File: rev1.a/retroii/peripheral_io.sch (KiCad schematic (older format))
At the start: 24 parts, among them J12 Peripheral Slot 0, J15 Peripheral Slot 4, J16 Peripheral Slot 1, J17 Peripheral Slot 5, J18 Peripheral Slot 2, J19 Peripheral Slot 6, J20 Peripheral Slot 3, J21 Peripheral Slot 7

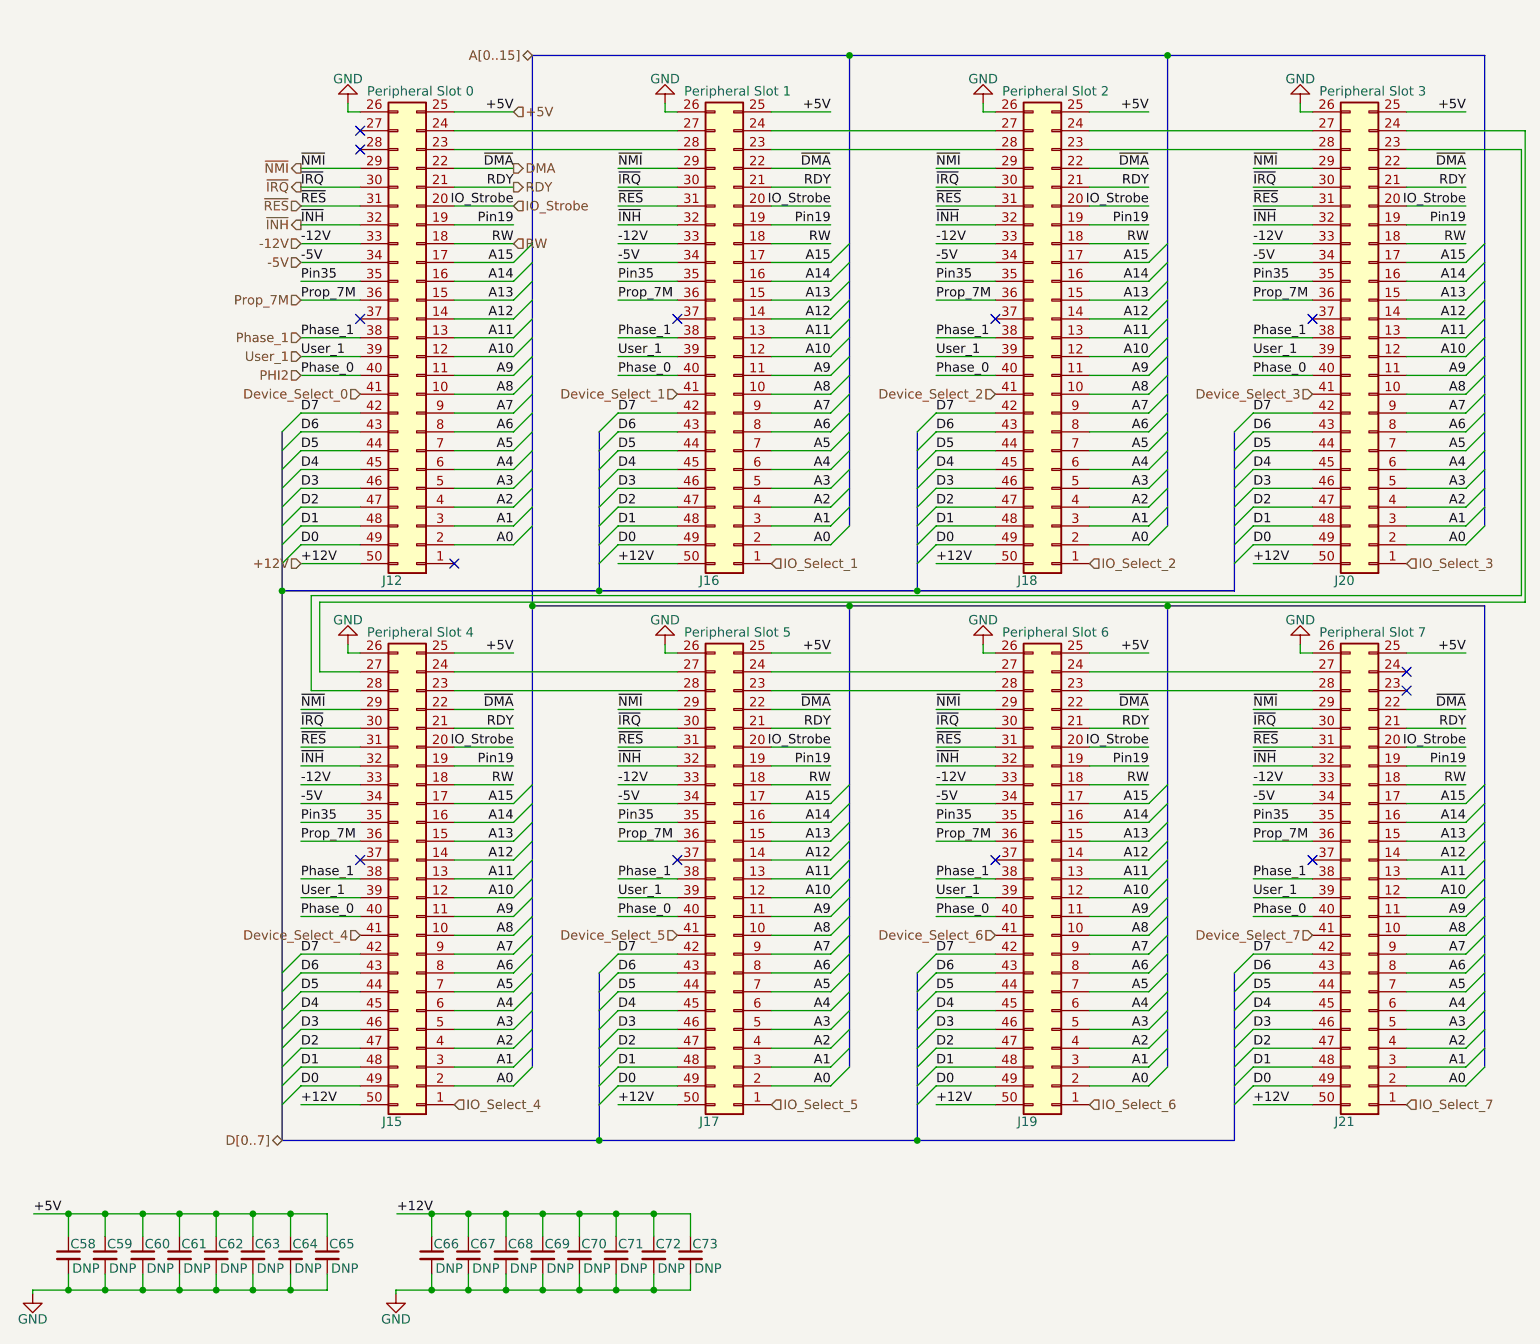
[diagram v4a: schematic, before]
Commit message: added prop_q3 to peripheral slot connections.
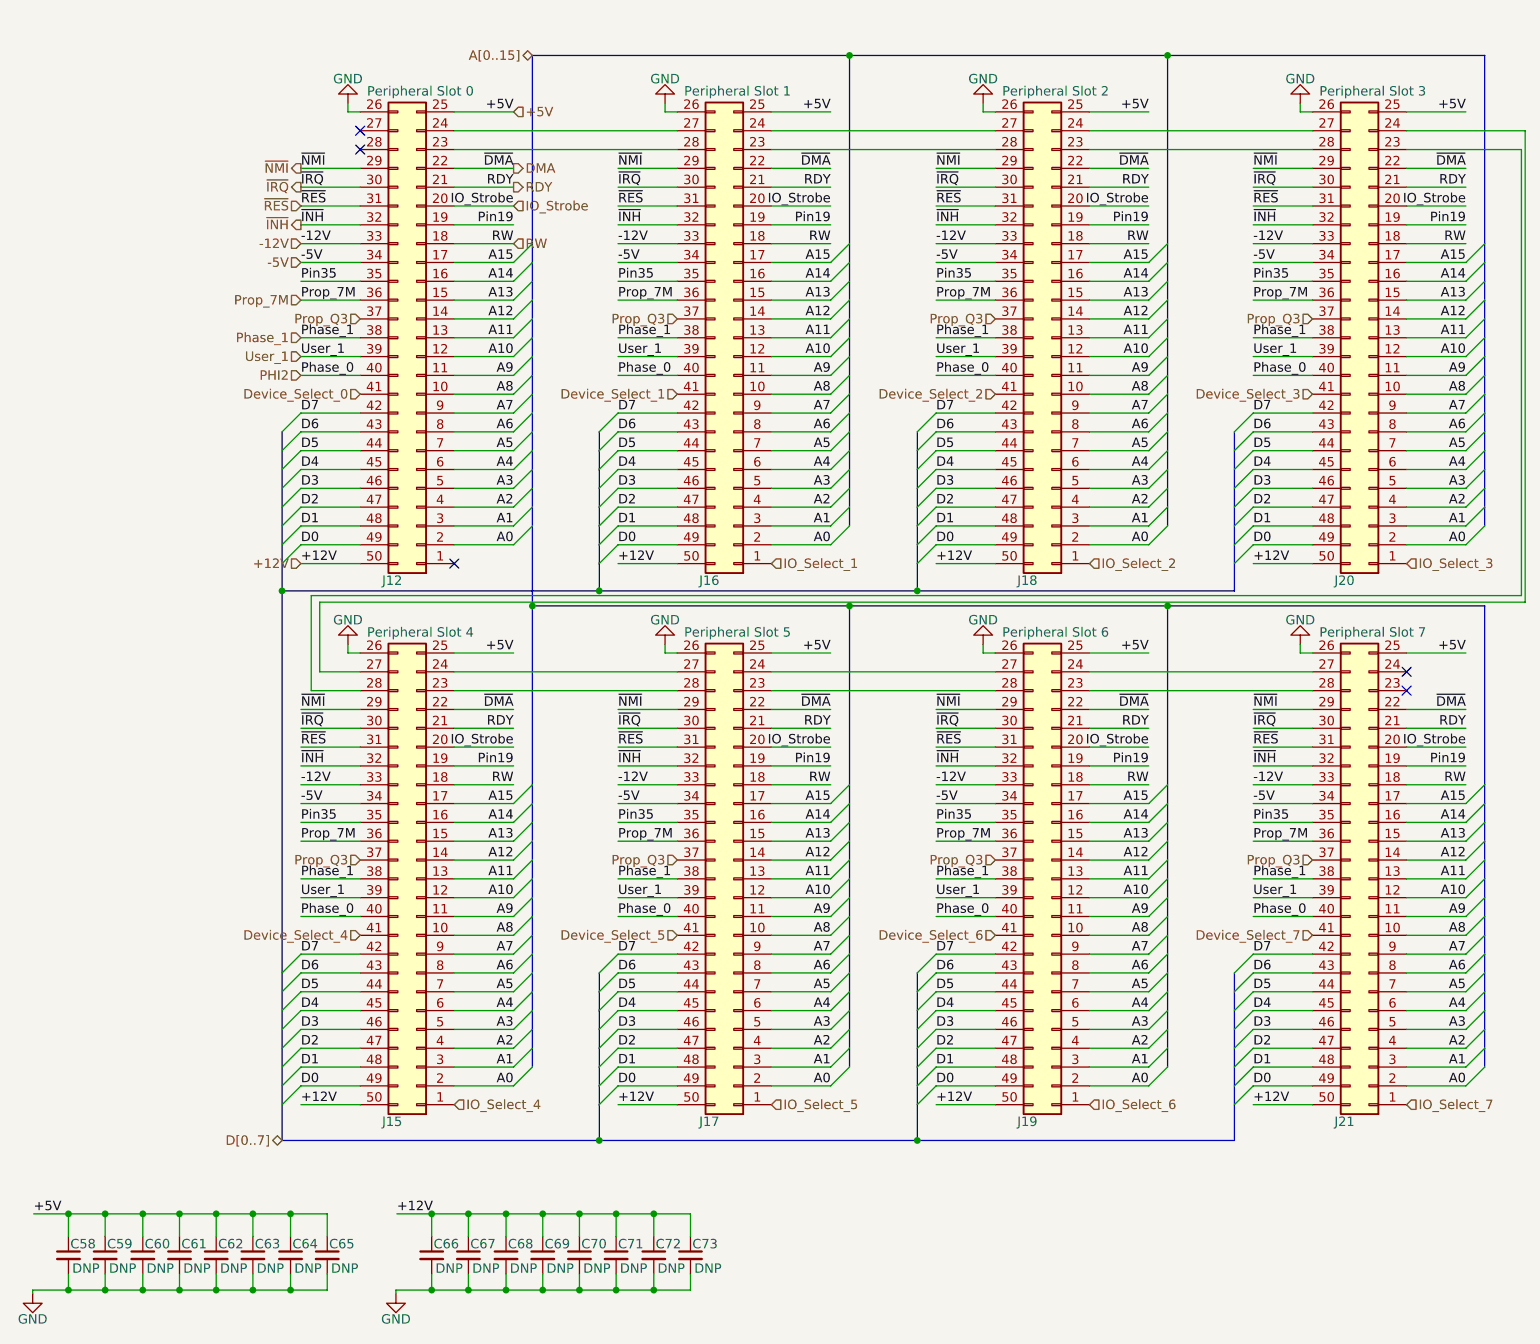
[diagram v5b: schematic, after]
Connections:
- net Prop_Q3: now reaches J12.37 (Pin_37)
- net Prop_Q3: now also J15.37 (Pin_37), J16.37 (Pin_37), J17.37 (Pin_37), J18.37 (Pin_37), J19.37 (Pin_37), J20.37 (Pin_37), J21.37 (Pin_37)
- no-connect marks 13 -> 5
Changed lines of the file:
@@
 Text Label 2545 2225 0    50   ~ 0
 Phase_1
-NoConn ~ 2860 2125
 Entry Wire Line
 	3675 1825 3775 1725
@@
 Text Label 4230 2225 0    50   ~ 0
 Phase_1
-NoConn ~ 4545 2125
 Entry Wire Line
 	5360 1825 5460 1725
@@
 Text Label 5920 2225 0    50   ~ 0
 Phase_1
-NoConn ~ 6235 2125
 Entry Wire Line
 	7050 1825 7150 1725
@@
 Text Label 7605 2225 0    50   ~ 0
 Phase_1
-NoConn ~ 7920 2125
 Entry Wire Line
 	8735 1825 8835 1725
@@
 Text Label 2545 5100 0    50   ~ 0
 Phase_1
-NoConn ~ 2860 5000
 Entry Wire Line
 	3675 4700 3775 4600
@@
 Text Label 4230 5100 0    50   ~ 0
 Phase_1
-NoConn ~ 4545 5000
 Entry Wire Line
 	5360 4700 5460 4600
@@
 Text Label 5920 5100 0    50   ~ 0
 Phase_1
-NoConn ~ 6235 5000
 Entry Wire Line
 	7050 4700 7150 4600
@@
 Text Label 7605 5100 0    50   ~ 0
 Phase_1
-NoConn ~ 7920 5000
 Entry Wire Line
 	8735 4700 8835 4600
@@
 Wire Bus Line
 	3775 725  3775 3650
+Text HLabel 2860 2125 0    50   Input ~ 0
+Prop_Q3
+Text HLabel 4545 2125 0    50   Input ~ 0
+Prop_Q3
+Text HLabel 6235 2125 0    50   Input ~ 0
+Prop_Q3
+Text HLabel 7920 2125 0    50   Input ~ 0
+Prop_Q3
+Text HLabel 7920 5000 0    50   Input ~ 0
+Prop_Q3
+Text HLabel 6235 5000 0    50   Input ~ 0
+Prop_Q3
+Text HLabel 4545 5000 0    50   Input ~ 0
+Prop_Q3
+Text HLabel 2860 5000 0    50   Input ~ 0
+Prop_Q3
 $EndSCHEMATC
